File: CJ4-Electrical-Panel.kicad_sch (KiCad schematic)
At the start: 43 parts, among them J1 Conn_01x03, J2 Conn_01x03, J3 Conn_01x03, J4 Conn_01x03, J5 Conn_01x03, J6 Conn_01x03, J7 USB_B_Mini, J8 AVR-ISP-6, U1 ATmega32U4-A, Y1 16MHz

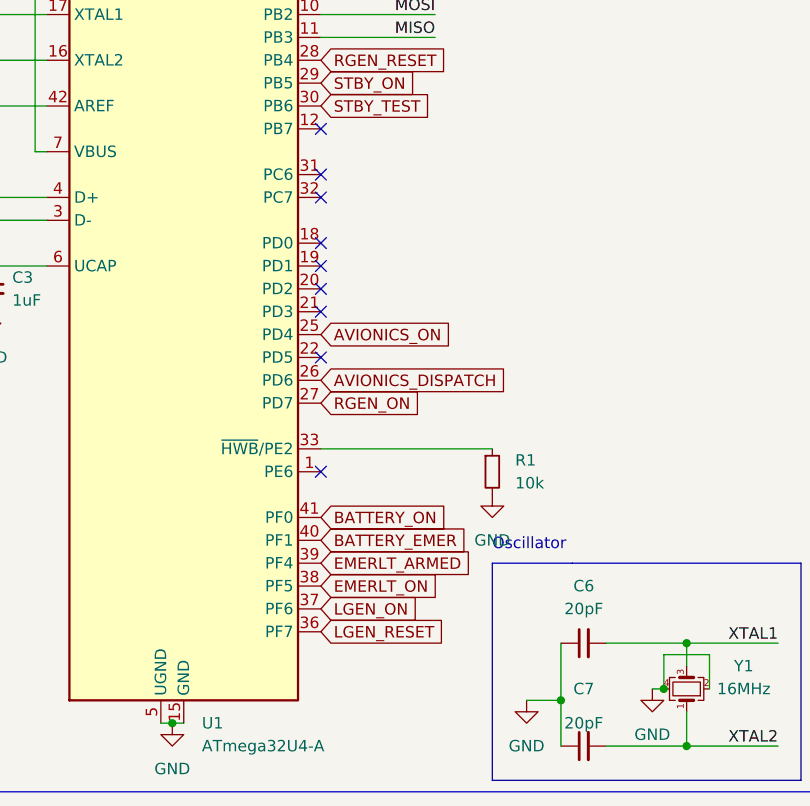
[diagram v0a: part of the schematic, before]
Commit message: All routed and ready for fab
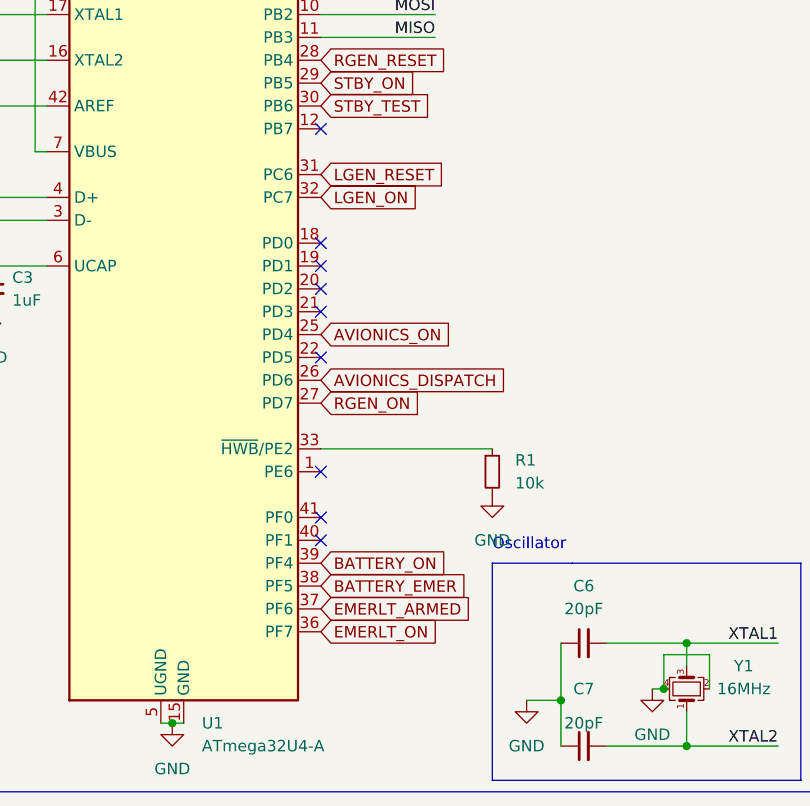
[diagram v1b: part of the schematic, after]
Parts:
- J1, J2, J3, J4, J5, J6: footprint Connector_JST:JST_XH_B3B-XH-AM_1x03_P2.50mm_Vertical -> Connector_JST:JST_XH_B3B-XH-A_1x03_P2.50mm_Vertical
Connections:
- net BATTERY_EMER: now also U1.38 (PF5); no longer U1.40 (PF1)
- net BATTERY_ON: now also U1.39 (PF4); no longer U1.41 (PF0)
- net EMERLT_ARMED: now also U1.37 (PF6); no longer U1.39 (PF4)
- net EMERLT_ON: now also U1.36 (PF7); no longer U1.38 (PF5)
- net LGEN_ON: now also U1.32 (PC7); no longer U1.37 (PF6)
- net LGEN_RESET: now also U1.31 (PC6); no longer U1.36 (PF7)
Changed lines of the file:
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@@
   (junction (at 46.99 124.46) (diameter 0) (color 0 0 0 0)
   )
+  (no_connect (at 63.5 101.6))
+  (no_connect (at 63.5 104.14))
   (no_connect (at 134.62 36.83))
   (no_connect (at 63.5 83.82))
@@
   (no_connect (at 63.5 78.74))
   (no_connect (at 63.5 58.42))
-  (no_connect (at 63.5 63.5))
-  (no_connect (at 63.5 66.04))
   (no_connect (at 63.5 71.12))
   (no_connect (at 63.5 73.66))
@@
     (effects (font (size 1.27 1.27)) (justify right bottom))
   )
-  (global_label "LGEN_ON" (shape input) (at 63.5 111.76 0) (fields_autoplaced)
-    (effects (font (size 1.27 1.27)) (justify left))
-    (property "Intersheet References" "${INTERSHEET_REFS}" (id 0) (at 74.3193 111.6806 0)
+  (global_label "LGEN_ON" (shape input) (at 63.5 66.04 0) (fields_autoplaced)
+    (effects (font (size 1.27 1.27)) (justify left))
+    (property "Intersheet References" "${INTERSHEET_REFS}" (id 0) (at 74.3193 65.9606 0)
       (effects (font (size 1.27 1.27)) (justify left) hide)
     )
@@
     )
   )
-  (global_label "LGEN_RESET" (shape input) (at 63.5 114.3 0) (fields_autoplaced)
-    (effects (font (size 1.27 1.27)) (justify left))
-    (property "Intersheet References" "${INTERSHEET_REFS}" (id 0) (at 77.4036 114.2206 0)
+  (global_label "LGEN_RESET" (shape input) (at 63.5 63.5 0) (fields_autoplaced)
+    (effects (font (size 1.27 1.27)) (justify left))
+    (property "Intersheet References" "${INTERSHEET_REFS}" (id 0) (at 77.4036 63.4206 0)
       (effects (font (size 1.27 1.27)) (justify left) hide)
     )
@@
     )
   )
-  (global_label "EMERLT_ARMED" (shape input) (at 63.5 106.68 0) (fields_autoplaced)
-    (effects (font (size 1.27 1.27)) (justify left))
-    (property "Intersheet References" "${INTERSHEET_REFS}" (id 0) (at 80.125 106.6006 0)
-      (effects (font (size 1.27 1.27)) (justify left) hide)
-    )
-  )
-  (global_label "BATTERY_ON" (shape input) (at 63.5 101.6 0) (fields_autoplaced)
-    (effects (font (size 1.27 1.27)) (justify left))
-    (property "Intersheet References" "${INTERSHEET_REFS}" (id 0) (at 77.3431 101.5206 0)
+  (global_label "EMERLT_ARMED" (shape input) (at 63.5 111.76 0) (fields_autoplaced)
+    (effects (font (size 1.27 1.27)) (justify left))
+    (property "Intersheet References" "${INTERSHEET_REFS}" (id 0) (at 80.125 111.6806 0)
+      (effects (font (size 1.27 1.27)) (justify left) hide)
+    )
+  )
+  (global_label "BATTERY_ON" (shape input) (at 63.5 106.68 0) (fields_autoplaced)
+    (effects (font (size 1.27 1.27)) (justify left))
+    (property "Intersheet References" "${INTERSHEET_REFS}" (id 0) (at 77.3431 106.6006 0)
       (effects (font (size 1.27 1.27)) (justify left) hide)
     )
@@
     )
   )
-  (global_label "BATTERY_EMER" (shape input) (at 63.5 104.14 0) (fields_autoplaced)
-    (effects (font (size 1.27 1.27)) (justify left))
-    (property "Intersheet References" "${INTERSHEET_REFS}" (id 0) (at 79.7017 104.0606 0)
+  (global_label "BATTERY_EMER" (shape input) (at 63.5 109.22 0) (fields_autoplaced)
+    (effects (font (size 1.27 1.27)) (justify left))
+    (property "Intersheet References" "${INTERSHEET_REFS}" (id 0) (at 79.7017 109.1406 0)
       (effects (font (size 1.27 1.27)) (justify left) hide)
     )
@@
     )
   )
-  (global_label "EMERLT_ON" (shape input) (at 63.5 109.22 0) (fields_autoplaced)
-    (effects (font (size 1.27 1.27)) (justify left))
-    (property "Intersheet References" "${INTERSHEET_REFS}" (id 0) (at 76.5569 109.1406 0)
+  (global_label "EMERLT_ON" (shape input) (at 63.5 114.3 0) (fields_autoplaced)
+    (effects (font (size 1.27 1.27)) (justify left))
+    (property "Intersheet References" "${INTERSHEET_REFS}" (id 0) (at 76.5569 114.2206 0)
       (effects (font (size 1.27 1.27)) (justify left) hide)
     )
@@
     (property "Reference" "J3" (id 0) (at 48.26 139.7 0))
     (property "Value" "Conn_01x03" (id 1) (at 48.26 142.24 0))
-    (property "Footprint" "Connector_JST:JST_XH_B3B-XH-AM_1x03_P2.50mm_Vertical" (id 2) (at 48.26 148.59 0)
+    (property "Footprint" "Connector_JST:JST_XH_B3B-XH-A_1x03_P2.50mm_Vertical" (id 2) (at 48.26 148.59 0)
       (effects (font (size 1.27 1.27)) hide)
     )
@@
     (property "Reference" "J1" (id 0) (at 22.86 139.7 0))
     (property "Value" "Conn_01x03" (id 1) (at 22.86 142.24 0))
-    (property "Footprint" "Connector_JST:JST_XH_B3B-XH-AM_1x03_P2.50mm_Vertical" (id 2) (at 22.86 148.59 0)
+    (property "Footprint" "Connector_JST:JST_XH_B3B-XH-A_1x03_P2.50mm_Vertical" (id 2) (at 22.86 148.59 0)
       (effects (font (size 1.27 1.27)) hide)
     )
@@
     (property "Reference" "J2" (id 0) (at 22.86 156.21 0))
     (property "Value" "Conn_01x03" (id 1) (at 22.86 158.75 0))
-    (property "Footprint" "Connector_JST:JST_XH_B3B-XH-AM_1x03_P2.50mm_Vertical" (id 2) (at 22.86 165.1 0)
+    (property "Footprint" "Connector_JST:JST_XH_B3B-XH-A_1x03_P2.50mm_Vertical" (id 2) (at 22.86 165.1 0)
       (effects (font (size 1.27 1.27)) hide)
     )
@@
     (property "Reference" "J6" (id 0) (at 74.93 156.21 0))
     (property "Value" "Conn_01x03" (id 1) (at 74.93 158.75 0))
-    (property "Footprint" "Connector_JST:JST_XH_B3B-XH-AM_1x03_P2.50mm_Vertical" (id 2) (at 74.93 165.1 0)
+    (property "Footprint" "Connector_JST:JST_XH_B3B-XH-A_1x03_P2.50mm_Vertical" (id 2) (at 74.93 165.1 0)
       (effects (font (size 1.27 1.27)) hide)
     )
@@
     (property "Reference" "J4" (id 0) (at 48.26 156.21 0))
     (property "Value" "Conn_01x03" (id 1) (at 48.26 158.75 0))
-    (property "Footprint" "Connector_JST:JST_XH_B3B-XH-AM_1x03_P2.50mm_Vertical" (id 2) (at 48.26 165.1 0)
+    (property "Footprint" "Connector_JST:JST_XH_B3B-XH-A_1x03_P2.50mm_Vertical" (id 2) (at 48.26 165.1 0)
       (effects (font (size 1.27 1.27)) hide)
     )
@@
     (property "Reference" "J5" (id 0) (at 74.93 139.7 0))
     (property "Value" "Conn_01x03" (id 1) (at 74.93 142.24 0))
-    (property "Footprint" "Connector_JST:JST_XH_B3B-XH-AM_1x03_P2.50mm_Vertical" (id 2) (at 74.93 148.59 0)
+    (property "Footprint" "Connector_JST:JST_XH_B3B-XH-A_1x03_P2.50mm_Vertical" (id 2) (at 74.93 148.59 0)
       (effects (font (size 1.27 1.27)) hide)
     )
@@
     )
     (path "/80c82da8-3d49-4c20-9d33-d9790fe09efe"
-      (reference "J1") (unit 1) (value "Conn_01x03") (footprint "Connector_JST:JST_XH_B3B-XH-AM_1x03_P2.50mm_Vertical")
+      (reference "J1") (unit 1) (value "Conn_01x03") (footprint "Connector_JST:JST_XH_B3B-XH-A_1x03_P2.50mm_Vertical")
     )
     (path "/873b31ee-c2f5-4fc1-802d-856b1dfbfffc"
-      (reference "J2") (unit 1) (value "Conn_01x03") (footprint "Connector_JST:JST_XH_B3B-XH-AM_1x03_P2.50mm_Vertical")
+      (reference "J2") (unit 1) (value "Conn_01x03") (footprint "Connector_JST:JST_XH_B3B-XH-A_1x03_P2.50mm_Vertical")
     )
     (path "/558cf18e-838d-4e2f-a916-865cc321619b"
-      (reference "J3") (unit 1) (value "Conn_01x03") (footprint "Connector_JST:JST_XH_B3B-XH-AM_1x03_P2.50mm_Vertical")
+      (reference "J3") (unit 1) (value "Conn_01x03") (footprint "Connector_JST:JST_XH_B3B-XH-A_1x03_P2.50mm_Vertical")
     )
     (path "/b374e32d-38f9-425f-8643-4c1e1c65b701"
-      (reference "J4") (unit 1) (value "Conn_01x03") (footprint "Connector_JST:JST_XH_B3B-XH-AM_1x03_P2.50mm_Vertical")
+      (reference "J4") (unit 1) (value "Conn_01x03") (footprint "Connector_JST:JST_XH_B3B-XH-A_1x03_P2.50mm_Vertical")
     )
     (path "/e1108583-6a3a-4cc1-852c-a3d37fad7647"
-      (reference "J5") (unit 1) (value "Conn_01x03") (footprint "Connector_JST:JST_XH_B3B-XH-AM_1x03_P2.50mm_Vertical")
+      (reference "J5") (unit 1) (value "Conn_01x03") (footprint "Connector_JST:JST_XH_B3B-XH-A_1x03_P2.50mm_Vertical")
     )
     (path "/b363f36b-6e13-44a0-abfc-6b8406d73945"
-      (reference "J6") (unit 1) (value "Conn_01x03") (footprint "Connector_JST:JST_XH_B3B-XH-AM_1x03_P2.50mm_Vertical")
+      (reference "J6") (unit 1) (value "Conn_01x03") (footprint "Connector_JST:JST_XH_B3B-XH-A_1x03_P2.50mm_Vertical")
     )
     (path "/872f2b27-424b-40bd-8eb7-6befce0bc453"

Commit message: Correct footprint error, add USB render
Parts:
- D1: JLC SOD-232F -> SOD-323F
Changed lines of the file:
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@@
       (effects (font (size 1.27 1.27)) hide)
     )
-    (property "JLC" "SOD-232F" (id 4) (at 166.37 67.31 0)
+    (property "JLC" "SOD-323F" (id 4) (at 166.37 67.31 0)
       (effects (font (size 1.27 1.27)) hide)
     )

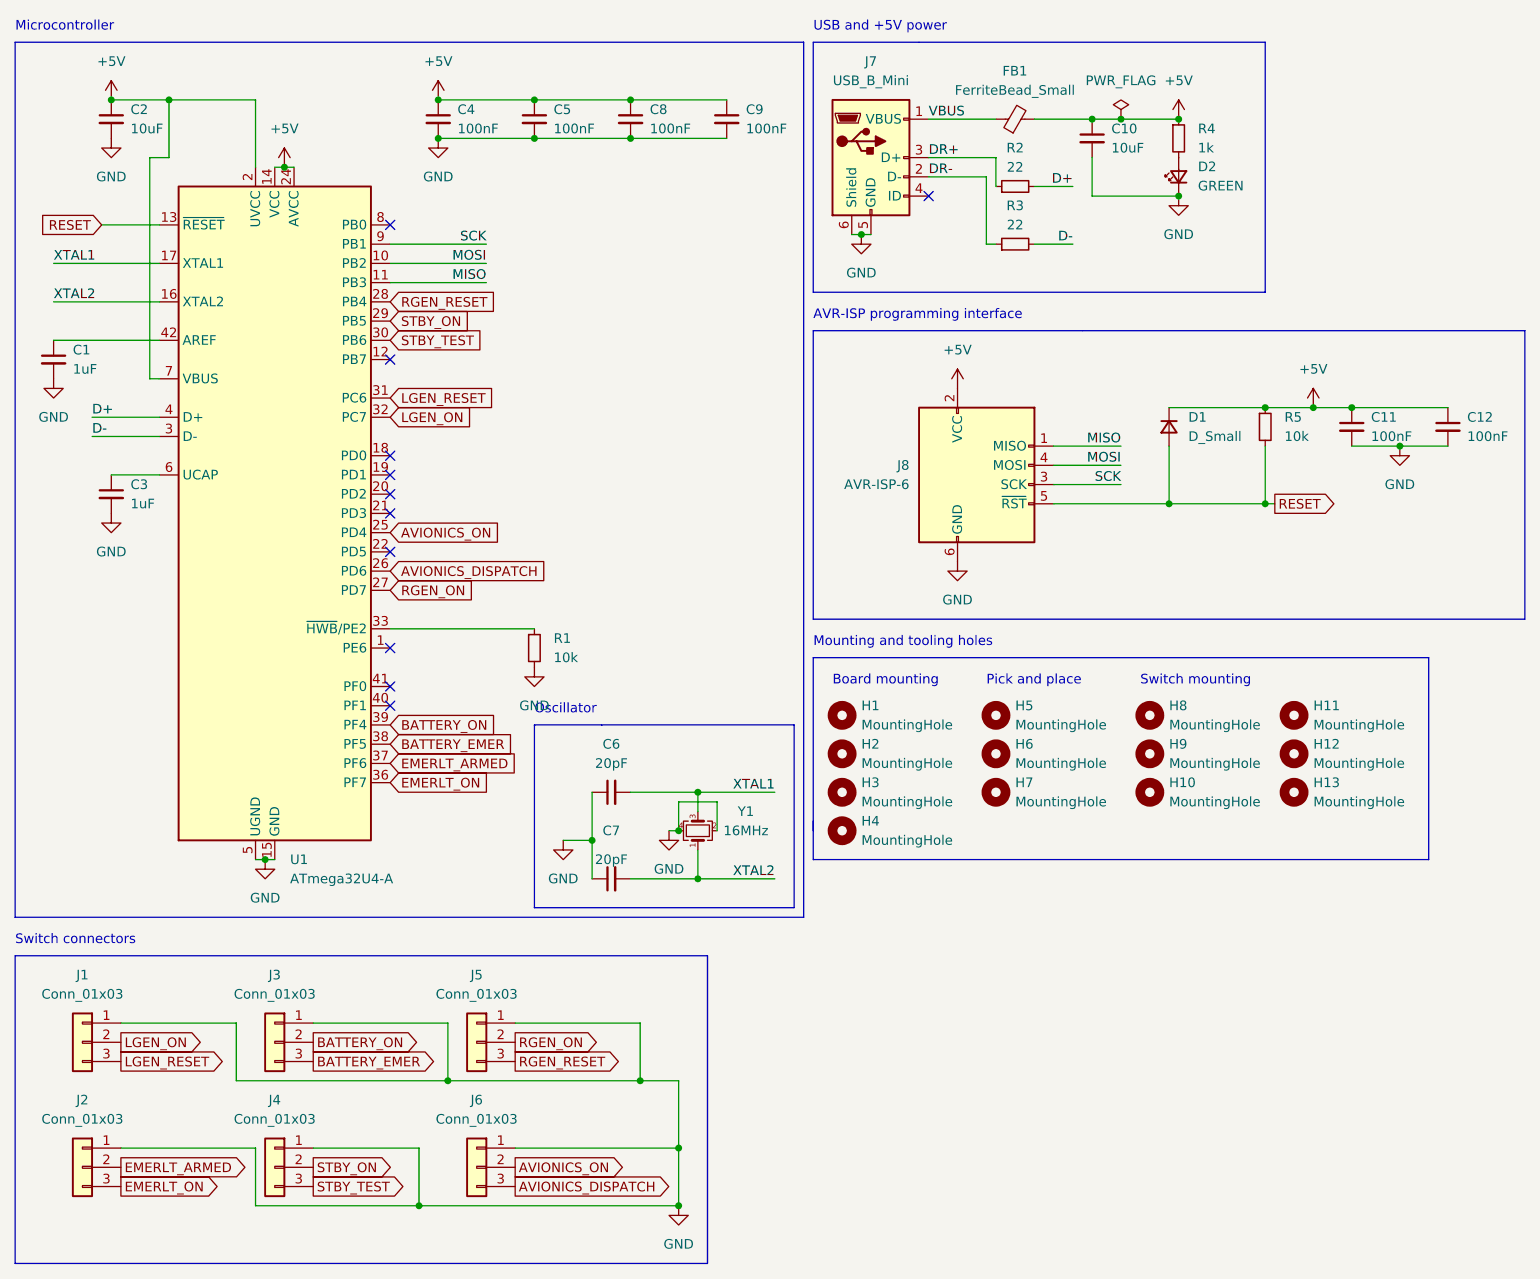
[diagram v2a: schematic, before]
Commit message: Change USB connector, add missing labels
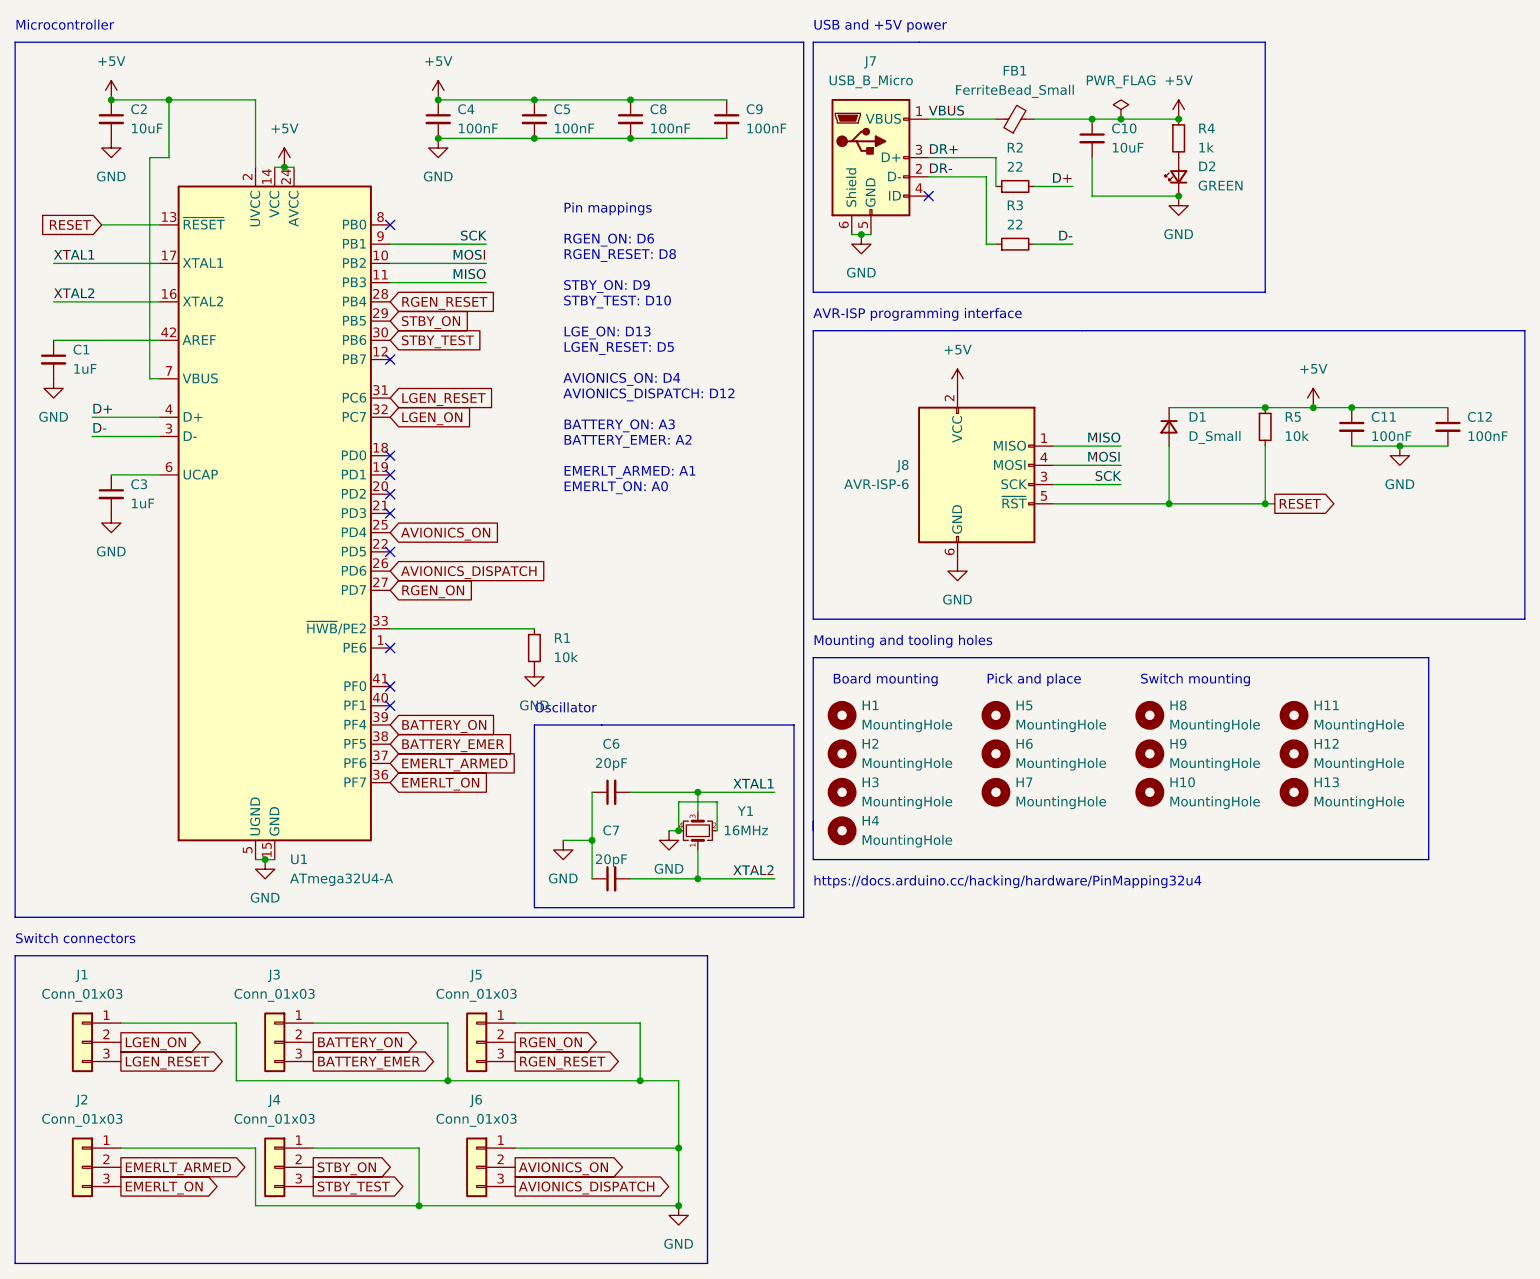
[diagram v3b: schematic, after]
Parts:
- removed J7: USB_B_Mini, CJ4-Electrical-Panel:ZX80-B-5P, symbol Connector:USB_B_Mini
- added J7: USB_B_Micro, CJ4-Electrical-Panel:USB_B_Mini_Amphenol_UE25BE5510H, symbol Connector:USB_B_Micro
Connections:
- net DR+: now also J7.3 (D+)
- net DR-: now also J7.2 (D-)
- net GND: now also J7.5 (GND), J7.6 (Shield)
- net VBUS: now also J7.1 (VBUS)
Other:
- note added: "Pin mappings RGEN_ON: D6 RGEN_RESET: D8 STBY_ON: D9 STBY_TEST: D10 LGE_ON: D13 LGEN_RESET: D5 AVIONICS_ON: D4 AVIONICS_DISPATCH: D12 BATTERY_ON: A3 BATTERY_EMER: A2 EMERLT_ARMED: A1 EMERLT_ON: A0"
- note added: "https://docs.arduino.cc/hacking/hardware/PinMapping32u4"
